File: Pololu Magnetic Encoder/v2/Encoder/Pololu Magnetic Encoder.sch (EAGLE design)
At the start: 8 parts, among them U1 AS5035

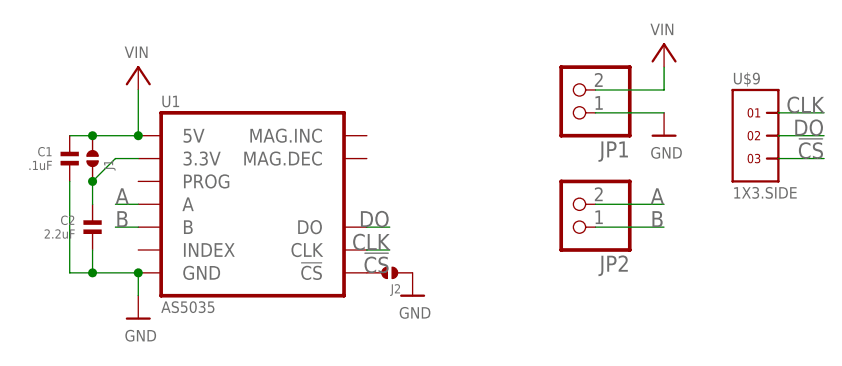
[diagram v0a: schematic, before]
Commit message: Updated Pololu Magnetic Encoder, fixing pullup issue and adding new silkscreen info
Signed-off-by: Cruz Monrreal II <Cruz.Monrreal@gmail.com>
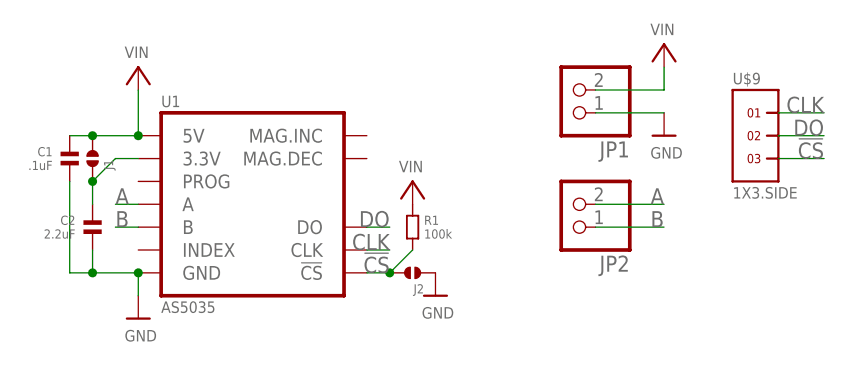
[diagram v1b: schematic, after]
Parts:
- added R1: 100k, .standardparts:RESISTOR.0603
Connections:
- removed net N$1: J2.2, U1.!CS
- net !CS: now also J2.2, R1.2, U1.!CS; no longer J2.1
- net GND: now also J2.1
- net VIN: now also R1.1
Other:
- moved on the sheet: J2
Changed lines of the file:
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@@
 <?xml version="1.0" encoding="utf-8"?>
 <!DOCTYPE eagle SYSTEM "eagle.dtd">
-<eagle version="6.1">
+<eagle version="6.3">
 <drawing>
 <settings>
@@
 <setting verticaltext="up"/>
 </settings>
-<grid distance="0.1" unitdist="inch" unit="inch" style="dots" multiple="1" display="yes" altdistance="0.01" altunitdist="inch" altunit="inch"/>
+<grid distance="0.1" unitdist="inch" unit="inch" style="lines" multiple="1" display="no" altdistance="0.01" altunitdist="inch" altunit="inch"/>
 <layers>
 <layer number="1" name="Top" color="4" fill="1" visible="no" active="no"/>
@@
 <part name="JP1" library="microbuilder" deviceset="HEADER-1X2" device="ROUND"/>
 <part name="JP2" library="microbuilder" deviceset="HEADER-1X2" device="ROUND"/>
+<part name="R1" library=".standardparts" deviceset="RESISTOR" device=".0603" value="100k"/>
+<part name="U$1" library="microbuilder" deviceset="VIN" device=""/>
 </parts>
 <sheets>
@@
 <instance part="U$2" gate="G$1" x="25.4" y="154.94"/>
 <instance part="U$3" gate="G$1" x="25.4" y="129.54"/>
-<instance part="U$4" gate="G$1" x="55.88" y="132.08"/>
-<instance part="J2" gate="G$1" x="53.34" y="134.62" rot="R180"/>
+<instance part="U$4" gate="G$1" x="58.42" y="132.08"/>
+<instance part="J2" gate="G$1" x="55.88" y="134.62" rot="R180"/>
 <instance part="U$7" gate="G$1" x="83.82" y="157.48"/>
 <instance part="U$8" gate="G$1" x="83.82" y="149.86"/>
@@
 <instance part="JP1" gate="G$1" x="73.66" y="154.94" rot="R180"/>
 <instance part="JP2" gate="G$1" x="73.66" y="142.24" rot="R180"/>
+<instance part="R1" gate="G$1" x="55.88" y="139.7" rot="R270"/>
+<instance part="U$1" gate="G$1" x="55.88" y="142.24"/>
 </instances>
 <busses>
@@
 <pinref part="JP1" gate="G$1" pin="2"/>
 <wire x1="76.2" y1="154.94" x2="83.82" y2="154.94" width="0.1524" layer="91"/>
+</segment>
+<segment>
+<pinref part="R1" gate="G$1" pin="1"/>
+<pinref part="U$1" gate="G$1" pin="VIN"/>
 </segment>
 </net>
@@
 <pinref part="U$8" gate="G$1" pin="GND"/>
 </segment>
-</net>
-<net name="!CS" class="0">
 <segment>
 <pinref part="J2" gate="G$1" pin="1"/>
 <pinref part="U$4" gate="G$1" pin="GND"/>
-<label x="53.34" y="134.62" size="1.778" layer="95" rot="MR0"/>
-</segment>
+</segment>
+</net>
+<net name="!CS" class="0">
 <segment>
 <pinref part="U$9" gate="G$1" pin="3"/>
 <wire x1="96.52" y1="147.32" x2="101.6" y2="147.32" width="0.1524" layer="91"/>
 <label x="101.6" y="147.32" size="1.778" layer="95" rot="MR0"/>
+</segment>
+<segment>
+<pinref part="J2" gate="G$1" pin="2"/>
+<pinref part="U1" gate="G$1" pin="!CS"/>
+<wire x1="53.34" y1="134.62" x2="50.8" y2="134.62" width="0.1524" layer="91"/>
+<wire x1="53.34" y1="134.62" x2="55.88" y2="137.16" width="0.1524" layer="91"/>
+<junction x="53.34" y="134.62"/>
+<pinref part="R1" gate="G$1" pin="2"/>
+<label x="53.34" y="134.62" size="1.778" layer="95" rot="MR0"/>
 </segment>
 </net>
@@
 </segment>
 </net>
-<net name="N$1" class="0">
-<segment>
-<pinref part="J2" gate="G$1" pin="2"/>
-<pinref part="U1" gate="G$1" pin="!CS"/>
-</segment>
-</net>
